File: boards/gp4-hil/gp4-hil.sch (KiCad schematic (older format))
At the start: 0 parts

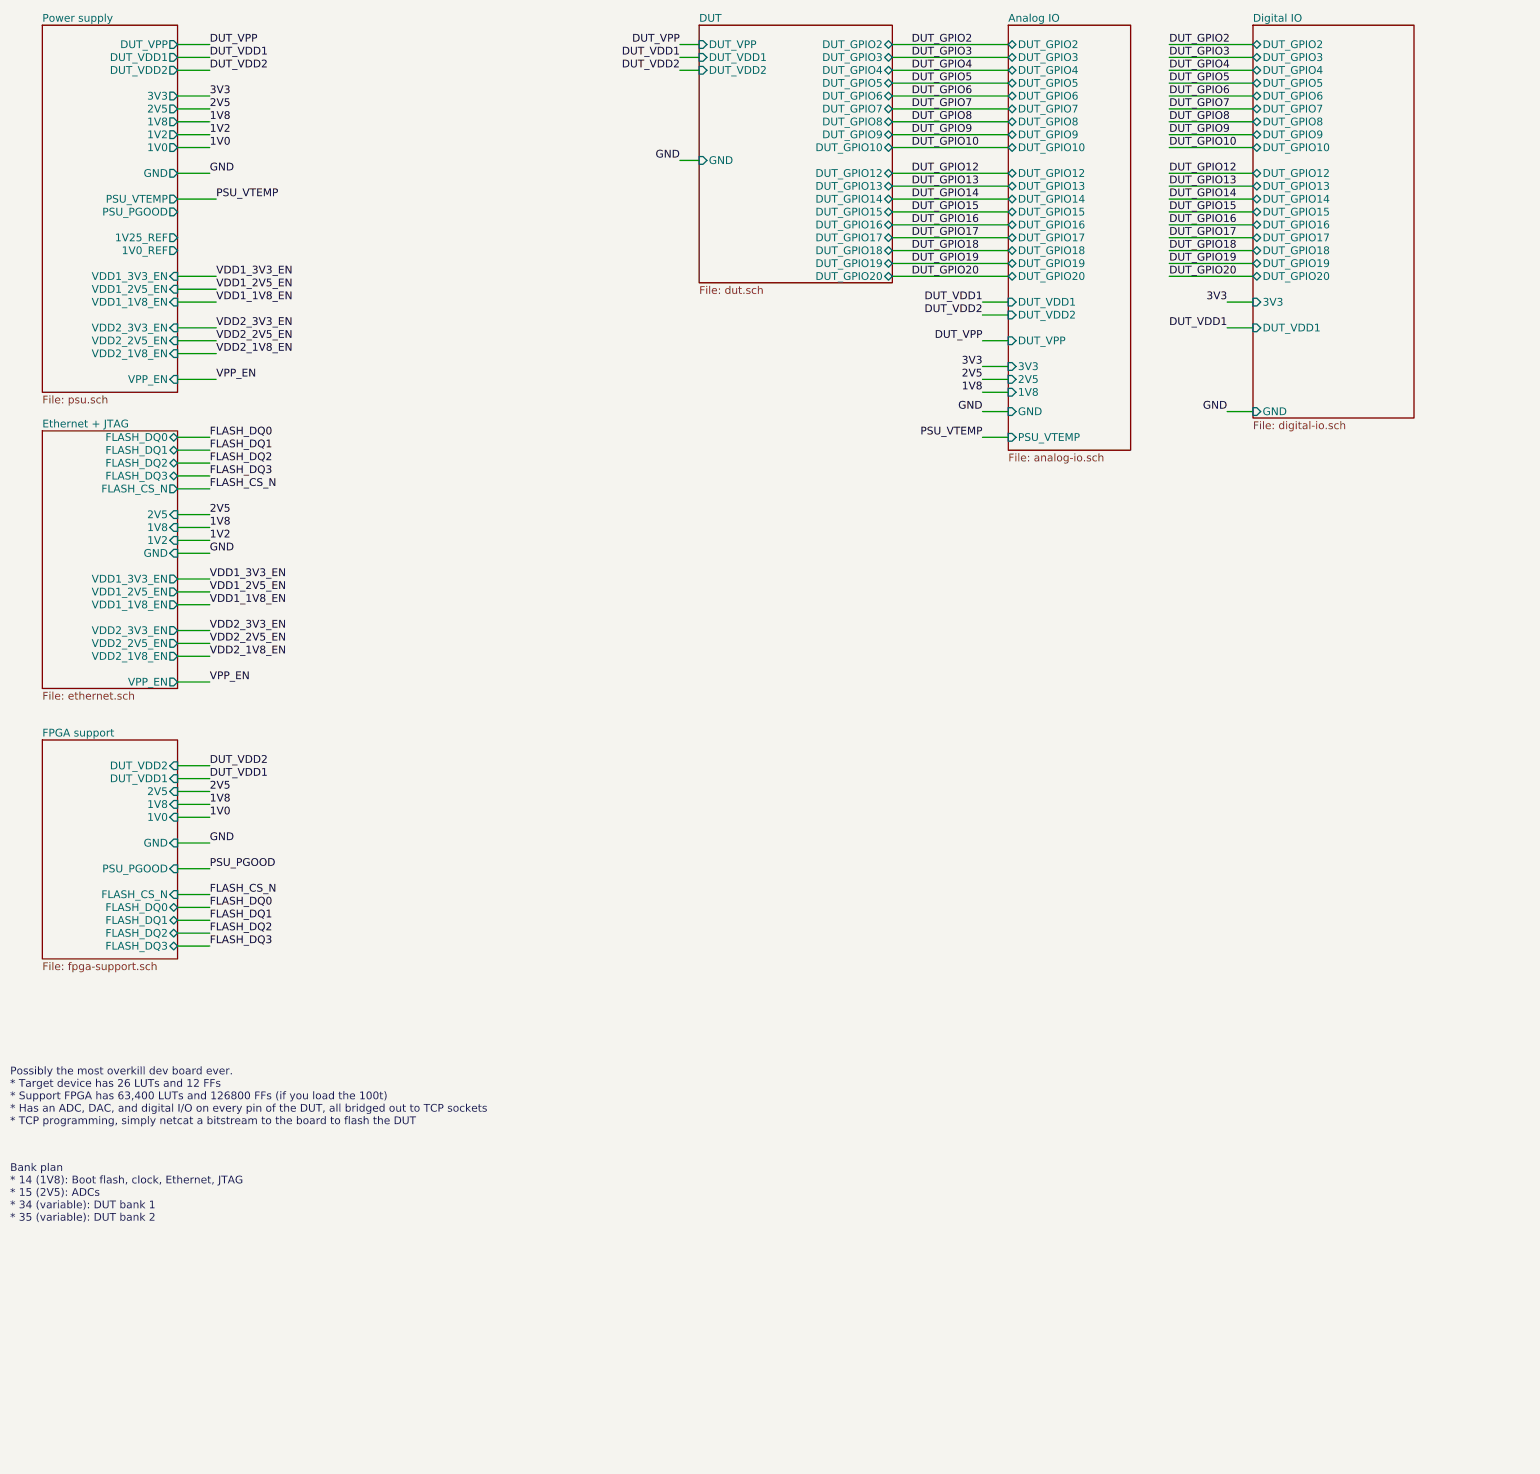
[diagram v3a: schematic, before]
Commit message: Added lots of analog I/O stuff
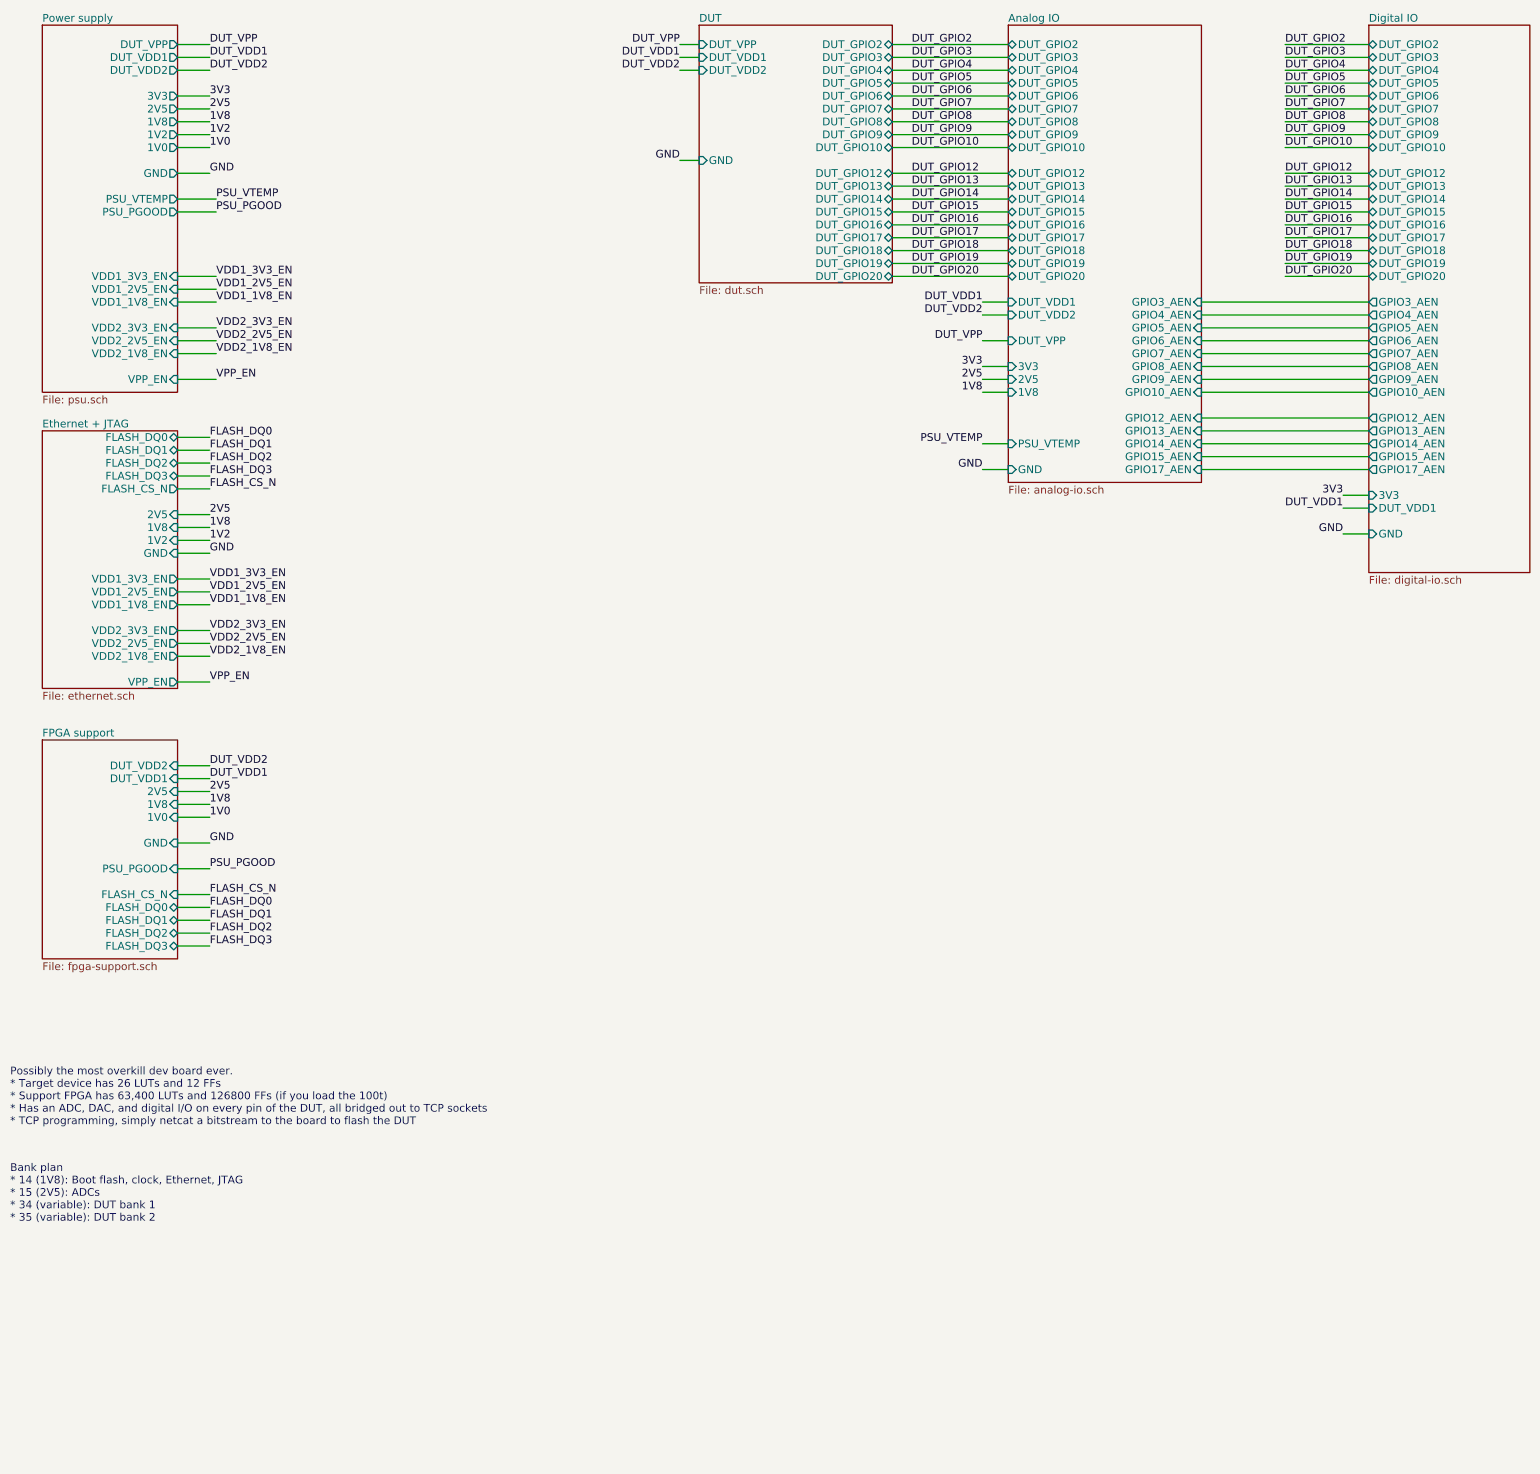
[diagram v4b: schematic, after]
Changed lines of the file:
@@
 F11 "PSU_VTEMP" O R 2550 2550 60
 F12 "PSU_PGOOD" O R 2550 2650 60
-F13 "1V25_REF" O R 2550 2850 60
-F14 "1V0_REF" O R 2550 2950 60
 F15 "VDD1_3V3_EN" I R 2550 3150 60
 F16 "VDD1_1V8_EN" I R 2550 3350 60
@@
 $EndSheet
 $Sheet
-S 9000 1200 950  3300
+S 9000 1200 1500 3550
 U 57316A68
 F0 "Analog IO" 60
@@
 F2 "DUT_VDD1" I L 9000 3350 60
 F3 "DUT_VDD2" I L 9000 3450 60
-F4 "GND" I L 9000 4200 60
+F4 "GND" I L 9000 4650 60
 F5 "DUT_VPP" I L 9000 3650 60
 F6 "DUT_GPIO2" B L 9000 1350 60
@@
 F25 "1V8" I L 9000 4050 60
 F26 "3V3" I L 9000 3850 60
-F27 "PSU_VTEMP" I L 9000 4400 60
+F27 "PSU_VTEMP" I L 9000 4450 60
+F28 "GPIO3_AEN" I R 10500 3350 60
+F29 "GPIO4_AEN" I R 10500 3450 60
+F30 "GPIO5_AEN" I R 10500 3550 60
+F31 "GPIO6_AEN" I R 10500 3650 60
+F32 "GPIO7_AEN" I R 10500 3750 60
+F33 "GPIO8_AEN" I R 10500 3850 60
+F34 "GPIO9_AEN" I R 10500 3950 60
+F35 "GPIO10_AEN" I R 10500 4050 60
+F36 "GPIO12_AEN" I R 10500 4250 60
+F37 "GPIO13_AEN" I R 10500 4350 60
+F38 "GPIO14_AEN" I R 10500 4450 60
+F39 "GPIO15_AEN" I R 10500 4550 60
+F40 "GPIO17_AEN" I R 10500 4650 60
 $EndSheet
 $Sheet
@@
 DUT_GPIO20
 $Sheet
-S 10900 1200 1250 3050
+S 11800 1200 1250 4250
 U 573AABB3
 F0 "Digital IO" 60
 F1 "digital-io.sch" 60
-F2 "GND" I L 10900 4200 60
-F3 "DUT_GPIO2" B L 10900 1350 60
-F4 "DUT_GPIO3" B L 10900 1450 60
-F5 "DUT_GPIO4" B L 10900 1550 60
-F6 "DUT_GPIO5" B L 10900 1650 60
-F7 "DUT_GPIO6" B L 10900 1750 60
-F8 "DUT_GPIO7" B L 10900 1850 60
-F9 "DUT_GPIO8" B L 10900 1950 60
-F10 "DUT_GPIO9" B L 10900 2050 60
-F11 "DUT_GPIO10" B L 10900 2150 60
-F12 "DUT_GPIO12" B L 10900 2350 60
-F13 "DUT_GPIO13" B L 10900 2450 60
-F14 "DUT_GPIO14" B L 10900 2550 60
-F15 "DUT_GPIO15" B L 10900 2650 60
-F16 "DUT_GPIO16" B L 10900 2750 60
-F17 "DUT_GPIO17" B L 10900 2850 60
-F18 "DUT_GPIO18" B L 10900 2950 60
-F19 "DUT_GPIO19" B L 10900 3050 60
-F20 "DUT_GPIO20" B L 10900 3150 60
-F21 "DUT_VDD1" I L 10900 3550 60
-F22 "3V3" I L 10900 3350 60
+F2 "GND" I L 11800 5150 60
+F3 "DUT_GPIO2" B L 11800 1350 60
+F4 "DUT_GPIO3" B L 11800 1450 60
+F5 "DUT_GPIO4" B L 11800 1550 60
+F6 "DUT_GPIO5" B L 11800 1650 60
+F7 "DUT_GPIO6" B L 11800 1750 60
+F8 "DUT_GPIO7" B L 11800 1850 60
+F9 "DUT_GPIO8" B L 11800 1950 60
+F10 "DUT_GPIO9" B L 11800 2050 60
+F11 "DUT_GPIO10" B L 11800 2150 60
+F12 "DUT_GPIO12" B L 11800 2350 60
+F13 "DUT_GPIO13" B L 11800 2450 60
+F14 "DUT_GPIO14" B L 11800 2550 60
+F15 "DUT_GPIO15" B L 11800 2650 60
+F16 "DUT_GPIO16" B L 11800 2750 60
+F17 "DUT_GPIO17" B L 11800 2850 60
+F18 "DUT_GPIO18" B L 11800 2950 60
+F19 "DUT_GPIO19" B L 11800 3050 60
+F20 "DUT_GPIO20" B L 11800 3150 60
+F21 "DUT_VDD1" I L 11800 4950 60
+F22 "3V3" I L 11800 4850 60
+F23 "GPIO3_AEN" O L 11800 3350 60
+F24 "GPIO4_AEN" O L 11800 3450 60
+F25 "GPIO5_AEN" O L 11800 3550 60
+F26 "GPIO6_AEN" O L 11800 3650 60
+F27 "GPIO7_AEN" O L 11800 3750 60
+F28 "GPIO8_AEN" O L 11800 3850 60
+F29 "GPIO9_AEN" O L 11800 3950 60
+F30 "GPIO10_AEN" O L 11800 4050 60
+F31 "GPIO12_AEN" O L 11800 4250 60
+F32 "GPIO13_AEN" O L 11800 4350 60
+F33 "GPIO14_AEN" O L 11800 4450 60
+F34 "GPIO15_AEN" O L 11800 4550 60
+F35 "GPIO17_AEN" O L 11800 4650 60
 $EndSheet
-Text Label 10250 1350 0    60   ~ 0
+Text Label 11150 1350 0    60   ~ 0
 DUT_GPIO2
-Text Label 10250 1450 0    60   ~ 0
+Text Label 11150 1450 0    60   ~ 0
 DUT_GPIO3
-Text Label 10250 1550 0    60   ~ 0
+Text Label 11150 1550 0    60   ~ 0
 DUT_GPIO4
-Text Label 10250 1650 0    60   ~ 0
+Text Label 11150 1650 0    60   ~ 0
 DUT_GPIO5
-Text Label 10250 1750 0    60   ~ 0
+Text Label 11150 1750 0    60   ~ 0
 DUT_GPIO6
-Text Label 10250 1850 0    60   ~ 0
+Text Label 11150 1850 0    60   ~ 0
 DUT_GPIO7
-Text Label 10250 1950 0    60   ~ 0
+Text Label 11150 1950 0    60   ~ 0
 DUT_GPIO8
-Text Label 10250 2050 0    60   ~ 0
+Text Label 11150 2050 0    60   ~ 0
 DUT_GPIO9
-Text Label 10250 2150 0    60   ~ 0
+Text Label 11150 2150 0    60   ~ 0
 DUT_GPIO10
-Text Label 10250 2350 0    60   ~ 0
+Text Label 11150 2350 0    60   ~ 0
 DUT_GPIO12
-Text Label 10250 2450 0    60   ~ 0
+Text Label 11150 2450 0    60   ~ 0
 DUT_GPIO13
-Text Label 10250 2550 0    60   ~ 0
+Text Label 11150 2550 0    60   ~ 0
 DUT_GPIO14
-Text Label 10250 2650 0    60   ~ 0
+Text Label 11150 2650 0    60   ~ 0
 DUT_GPIO15
-Text Label 10250 2750 0    60   ~ 0
+Text Label 11150 2750 0    60   ~ 0
 DUT_GPIO16
-Text Label 10250 2850 0    60   ~ 0
+Text Label 11150 2850 0    60   ~ 0
 DUT_GPIO17
-Text Label 10250 2950 0    60   ~ 0
+Text Label 11150 2950 0    60   ~ 0
 DUT_GPIO18
-Text Label 10250 3050 0    60   ~ 0
+Text Label 11150 3050 0    60   ~ 0
 DUT_GPIO19
-Text Label 10250 3150 0    60   ~ 0
+Text Label 11150 3150 0    60   ~ 0
 DUT_GPIO20
-Text Label 10700 4200 2    60   ~ 0
+Text Label 11600 5150 2    60   ~ 0
 GND
-Text Label 8800 4200 2    60   ~ 0
+Text Label 8800 4650 2    60   ~ 0
 GND
-Text Label 8800 4400 2    60   ~ 0
+Text Label 8800 4450 2    60   ~ 0
 PSU_VTEMP
 Text Label 2800 1350 0    60   ~ 0
@@
 	9000 3150 8100 3150
 Wire Wire Line
-	10250 1350 10900 1350
-Wire Wire Line
-	10900 1450 10250 1450
-Wire Wire Line
-	10250 1550 10900 1550
-Wire Wire Line
-	10900 1650 10250 1650
-Wire Wire Line
-	10250 1750 10900 1750
-Wire Wire Line
-	10900 1850 10250 1850
-Wire Wire Line
-	10250 1950 10900 1950
-Wire Wire Line
-	10900 2050 10250 2050
-Wire Wire Line
-	10250 2150 10900 2150
-Wire Wire Line
-	10900 2350 10250 2350
-Wire Wire Line
-	10900 2450 10250 2450
-Wire Wire Line
-	10900 2550 10250 2550
-Wire Wire Line
-	10250 2650 10900 2650
-Wire Wire Line
-	10900 2750 10250 2750
-Wire Wire Line
-	10900 2850 10250 2850
-Wire Wire Line
-	10250 2950 10900 2950
-Wire Wire Line
-	10900 3050 10250 3050
-Wire Wire Line
-	10250 3150 10900 3150
-Wire Wire Line
-	10700 4200 10900 4200
-Wire Wire Line
-	8800 4200 9000 4200
-Wire Wire Line
-	8800 4400 9000 4400
+	11150 1350 11800 1350
+Wire Wire Line
+	11800 1450 11150 1450
+Wire Wire Line
+	11150 1550 11800 1550
+Wire Wire Line
+	11800 1650 11150 1650
+Wire Wire Line
+	11150 1750 11800 1750
+Wire Wire Line
+	11800 1850 11150 1850
+Wire Wire Line
+	11150 1950 11800 1950
+Wire Wire Line
+	11800 2050 11150 2050
+Wire Wire Line
+	11150 2150 11800 2150
+Wire Wire Line
+	11800 2350 11150 2350
+Wire Wire Line
+	11800 2450 11150 2450
+Wire Wire Line
+	11800 2550 11150 2550
+Wire Wire Line
+	11150 2650 11800 2650
+Wire Wire Line
+	11800 2750 11150 2750
+Wire Wire Line
+	11800 2850 11150 2850
+Wire Wire Line
+	11150 2950 11800 2950
+Wire Wire Line
+	11800 3050 11150 3050
+Wire Wire Line
+	11150 3150 11800 3150
+Wire Wire Line
+	11600 5150 11800 5150
+Wire Wire Line
+	8800 4650 9000 4650
+Wire Wire Line
+	8800 4450 9000 4450
 Wire Wire Line
 	2800 1350 2550 1350
@@
 Wire Wire Line
 	8800 3450 9000 3450
-Text Label 10700 3350 2    60   ~ 0
+Text Label 11600 4850 2    60   ~ 0
 3V3
 Wire Wire Line
-	10700 3350 10900 3350
-Text Label 10700 3550 2    60   ~ 0
+	11600 4850 11800 4850
+Text Label 11600 4950 2    60   ~ 0
 DUT_VDD1
 Wire Wire Line
-	10700 3550 10900 3550
+	11600 4950 11800 4950
 Text Label 2850 3150 0    60   ~ 0
 VDD1_3V3_EN
@@
 Wire Wire Line
 	2800 8350 2550 8350
+Text Label 2850 2650 0    60   ~ 0
+PSU_PGOOD
+Wire Wire Line
+	2850 2650 2550 2650
+Wire Wire Line
+	10500 4050 11800 4050
+Wire Wire Line
+	11800 3950 10500 3950
+Wire Wire Line
+	10500 3850 11800 3850
+Wire Wire Line
+	11800 3750 10500 3750
+Wire Wire Line
+	10500 3650 11800 3650
+Wire Wire Line
+	11800 3550 10500 3550
+Wire Wire Line
+	10500 3450 11800 3450
+Wire Wire Line
+	11800 3350 10500 3350
+Wire Wire Line
+	11800 4650 10500 4650
+Wire Wire Line
+	10500 4550 11800 4550
+Wire Wire Line
+	11800 4450 10500 4450
+Wire Wire Line
+	10500 4350 11800 4350
+Wire Wire Line
+	11800 4250 10500 4250
 $EndSCHEMATC
